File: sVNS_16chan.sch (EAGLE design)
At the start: 55 parts, among them IC2 OPA990IDCKR, IC3 EFM8SB10F8A-A-QFN24EFM8SB10F8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, J1 M50-3631042, J2 M50-3631042, J3 M50-3631042, U1 NT3H2211W0FHKH, U2 LT8410EDC-1#TRMPBF, U3 MUX36S16IRSNR, U4 MUX36S16IRSNR

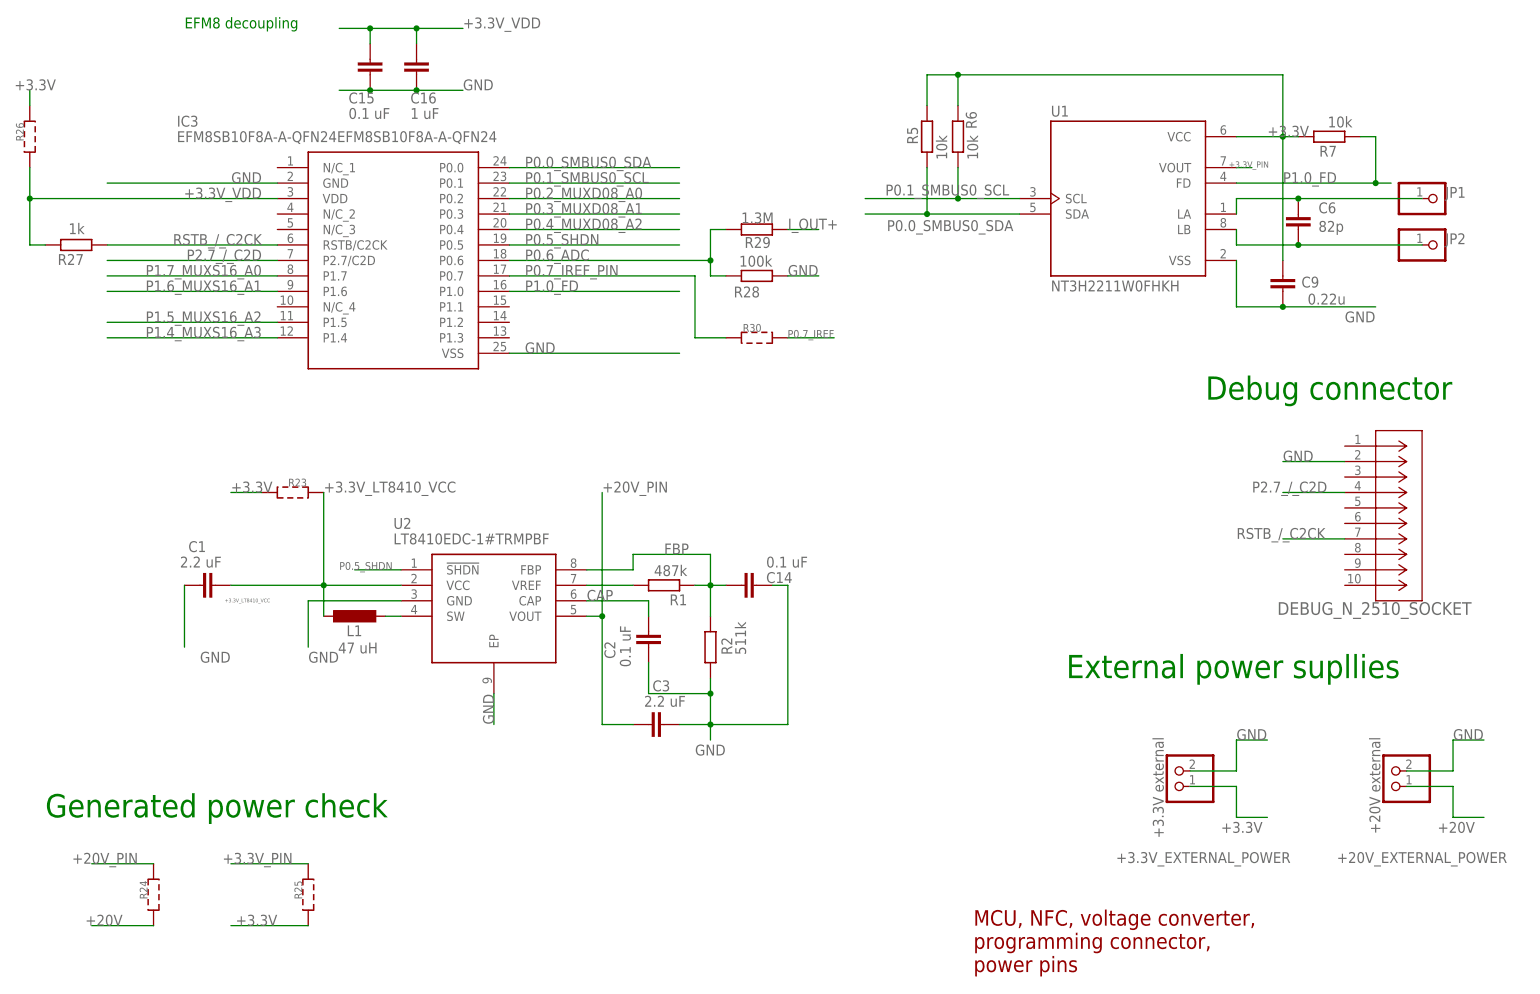
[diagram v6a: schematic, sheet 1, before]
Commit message: Checkpoint 3. Removed test pads on schematic. Ready for track retracing without the test pads. Existing wires preserved.
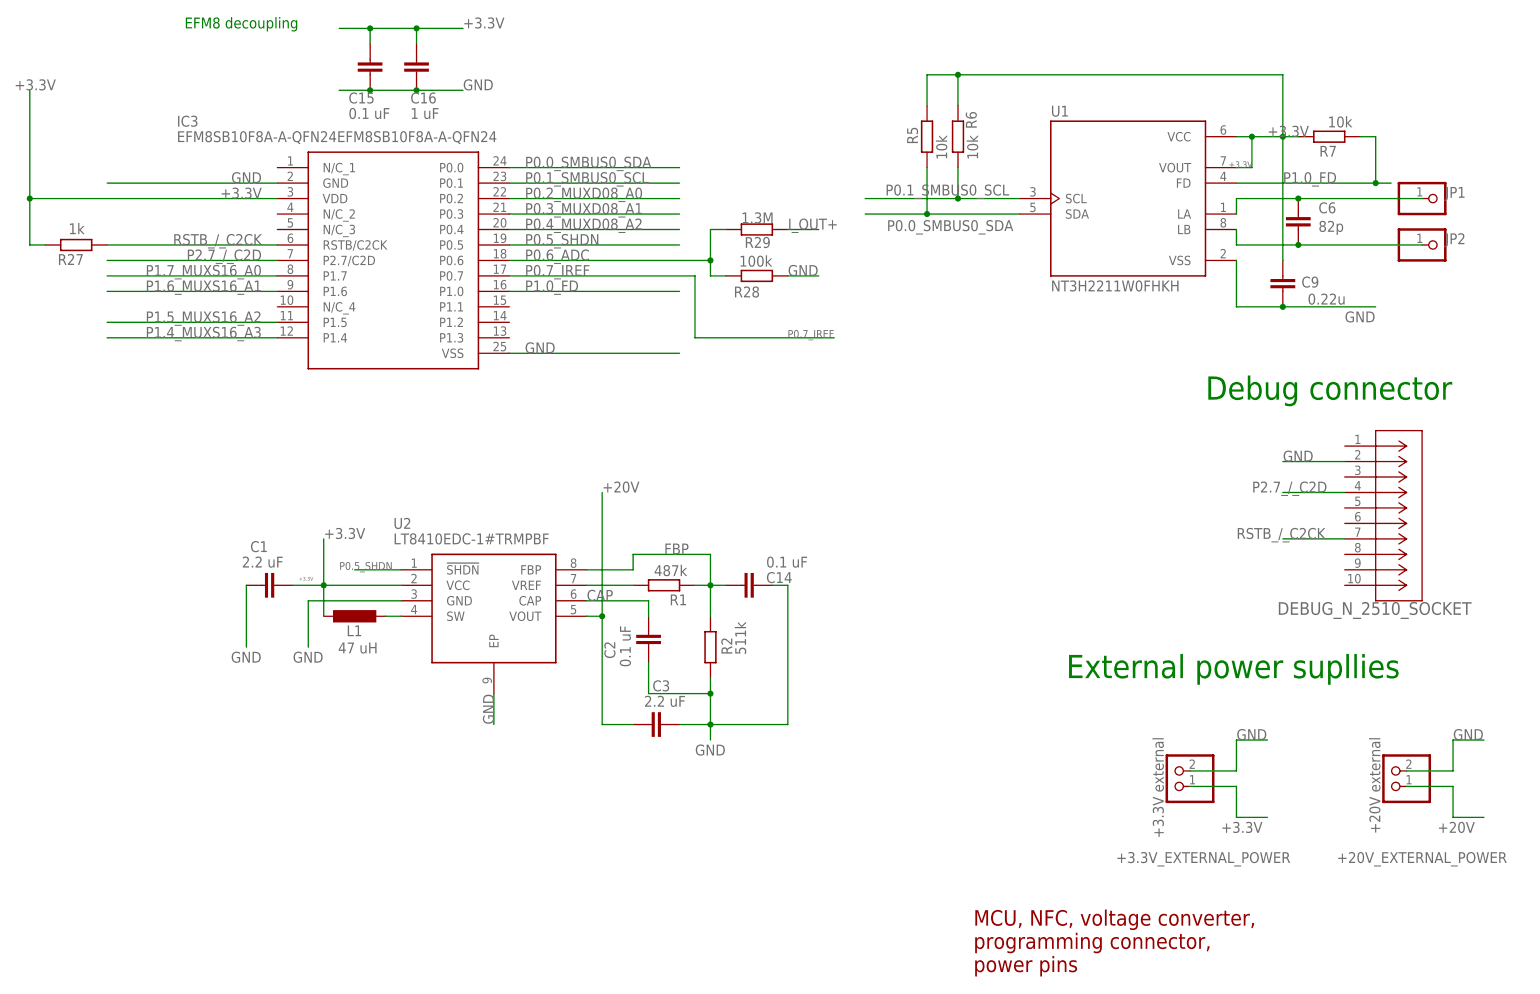
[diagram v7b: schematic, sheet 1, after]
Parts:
- removed R12, R14, R15, R16, R17, R18, R19, R20, R23, R24, R25, R26, R30: (no value), sVNS_16chan_lib:SMD_PADS_0603
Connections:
- removed net +20V_PIN: C3.1, R24.2, U2.VOUT
- removed net +3.3V_LT8410_VCC: C1.2, L1.1, R23.2, U2.VCC
- removed net +3.3V_PIN: R25.2, U1.VOUT
- removed net +3.3V_VDD: C15.2, C16.1, IC3.VDD, R26.1, R27.2
- removed net BAL_A_PIN: C4.2, R15.2
- removed net BAL_B_PIN: R13.2, R14.2
- removed net I_OUT+_PIN: IC2.OUT, R16.1
- removed net I_OUT-_PIN: C13.2, IC2.IN-, R10.2, R11.1, R18.1
- removed net MUX36D08_+20V: C11.2, R12.2, U$1.VDD
- removed net MUX36S16A+20V: C10.1, R19.2, U3.VDD
- removed net MUX36S16B_+20V: C5.2, R20.2, U4.VDD
- removed net OPAMP_+20V: C12.1, IC2.V+, R17.1
- removed net P0.7_IREF_PIN: IC3.P0.7, R30.2
- net +20V: now also C10.1, C11.2, C12.1, C3.1, C5.2, IC2.V+, U$1.VDD, U2.VOUT, U3.VDD, U4.VDD; no longer R12.1, R17.2, R19.1, R20.1, R24.1
- net +3.3V: now also C1.2, C15.2, C16.1, IC3.VDD, L1.1, R27.2, U1.VOUT, U2.VCC; no longer R23.1, R25.1, R26.2
- net BAL_A: now also C4.2; no longer R15.1
- net BAL_B: now also R13.2; no longer R14.1
- net I_OUT+: now also IC2.OUT; no longer R16.2
- net I_OUT-: now also C13.2, IC2.IN-, R10.2, R11.1; no longer R18.2
- net P0.7_IREF: now also IC3.P0.7; no longer R30.1
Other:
- note removed: "Generated power check"
- moved on the sheet: C1

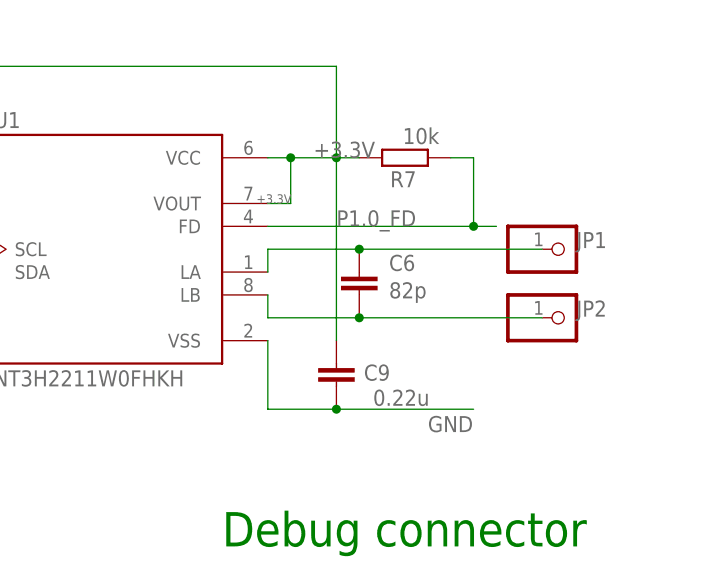
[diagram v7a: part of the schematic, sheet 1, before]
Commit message: Checkpoint 5. All unrouted traces finished. PCB optimised to 29.67 x 23.27.
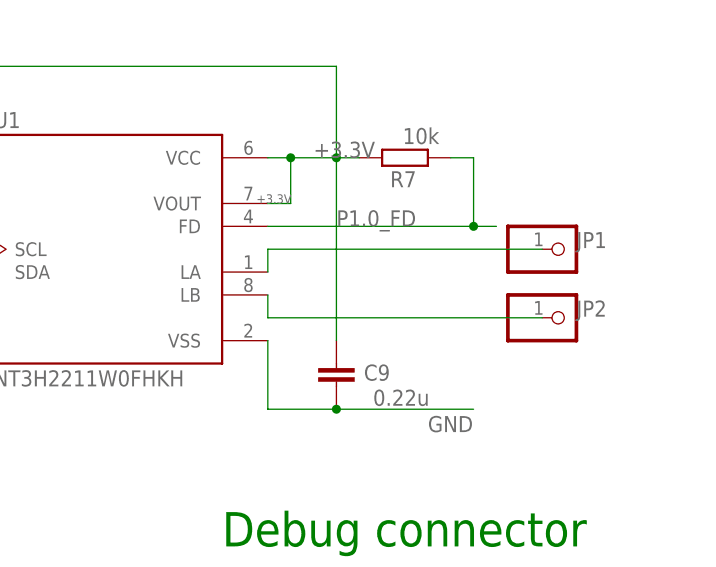
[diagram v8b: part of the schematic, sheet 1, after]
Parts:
- removed C6: 82p, rcl:C-EUC0402
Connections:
- net LA: no longer C6.1
- net LB: no longer C6.2
